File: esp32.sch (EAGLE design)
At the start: 14 parts, among them IC1 LM1117IMPX-3.3, U1 ESP32MOD

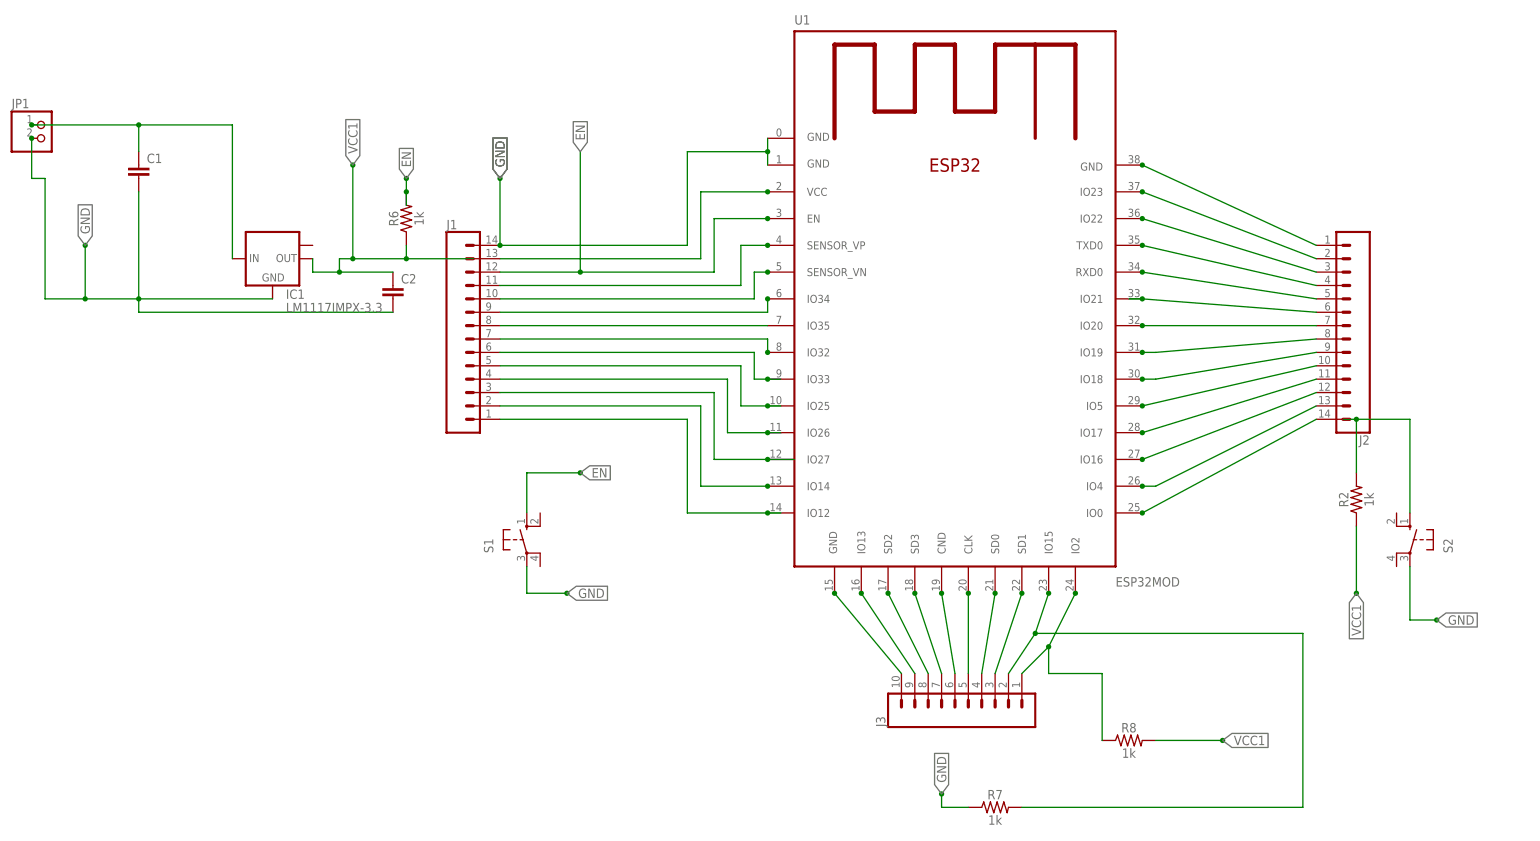
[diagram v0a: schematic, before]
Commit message: updated track and placing of AMS117 modified, peripheral: NA
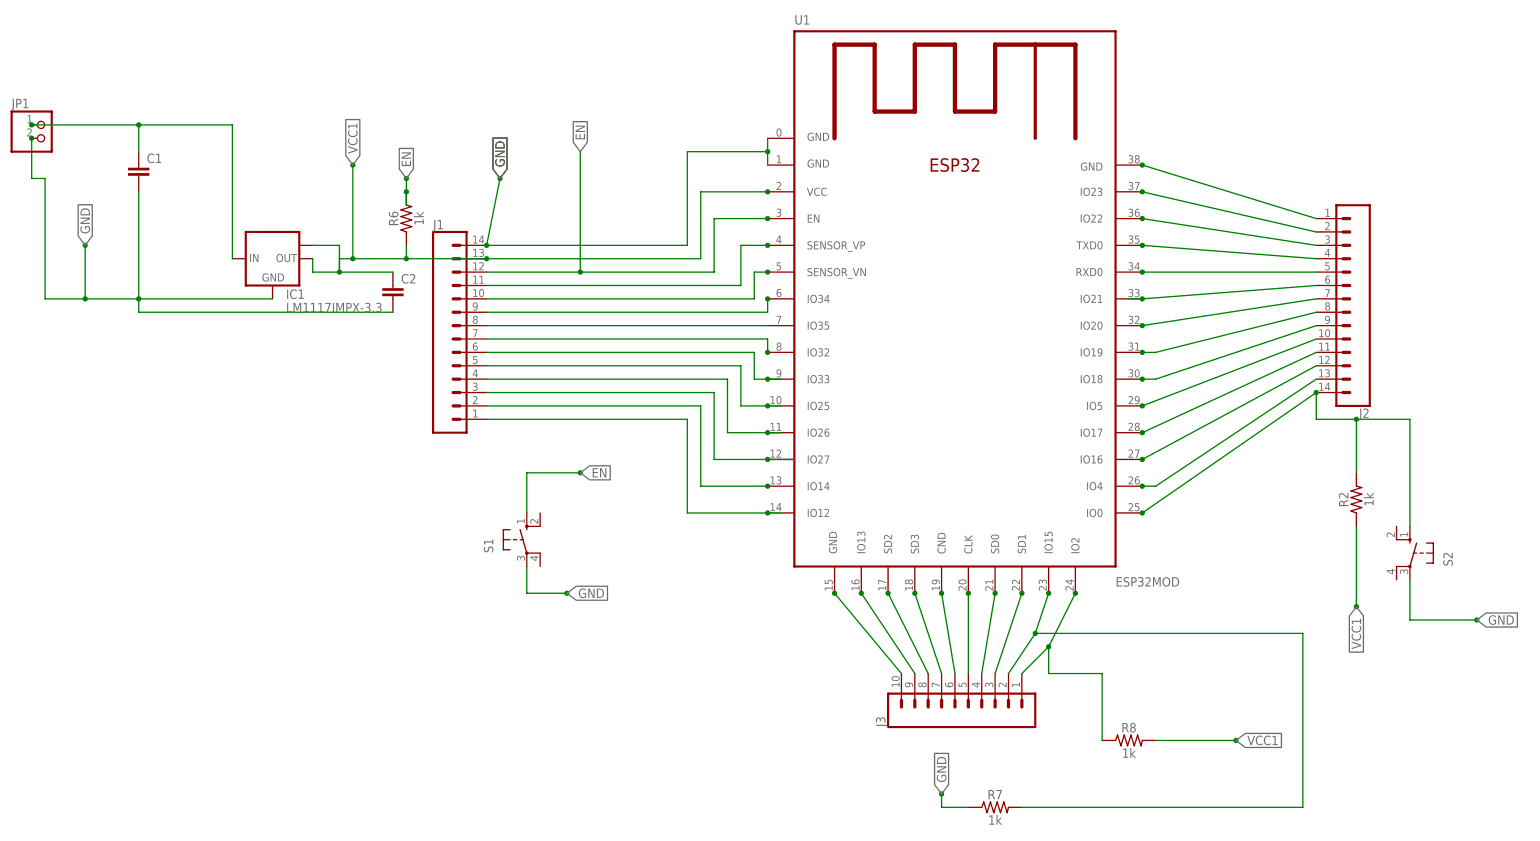
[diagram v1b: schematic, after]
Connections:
- removed net N$28: J2.14, U1.IO0
- removed net N$4: J1.13, U1.VCC
- net N$5: now also J2.14, U1.IO0
- net VCC1: now also IC1.OUT1, J1.13, U1.VCC
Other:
- moved on the sheet: J1, J2, S2
